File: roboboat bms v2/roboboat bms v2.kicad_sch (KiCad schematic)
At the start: 47 parts, among them J1 Conn_01x04_Pin, J2 XT90 Power Connector, J3 XT90 Power Connector, J4 BATT, J5 XT90 Power Connector, Q1 IRFP4468PbF, Q2 IRFP4468PbF, Q3 BSS84, Q4 IRFP4468PbF, Q5 IRFP4468PbF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

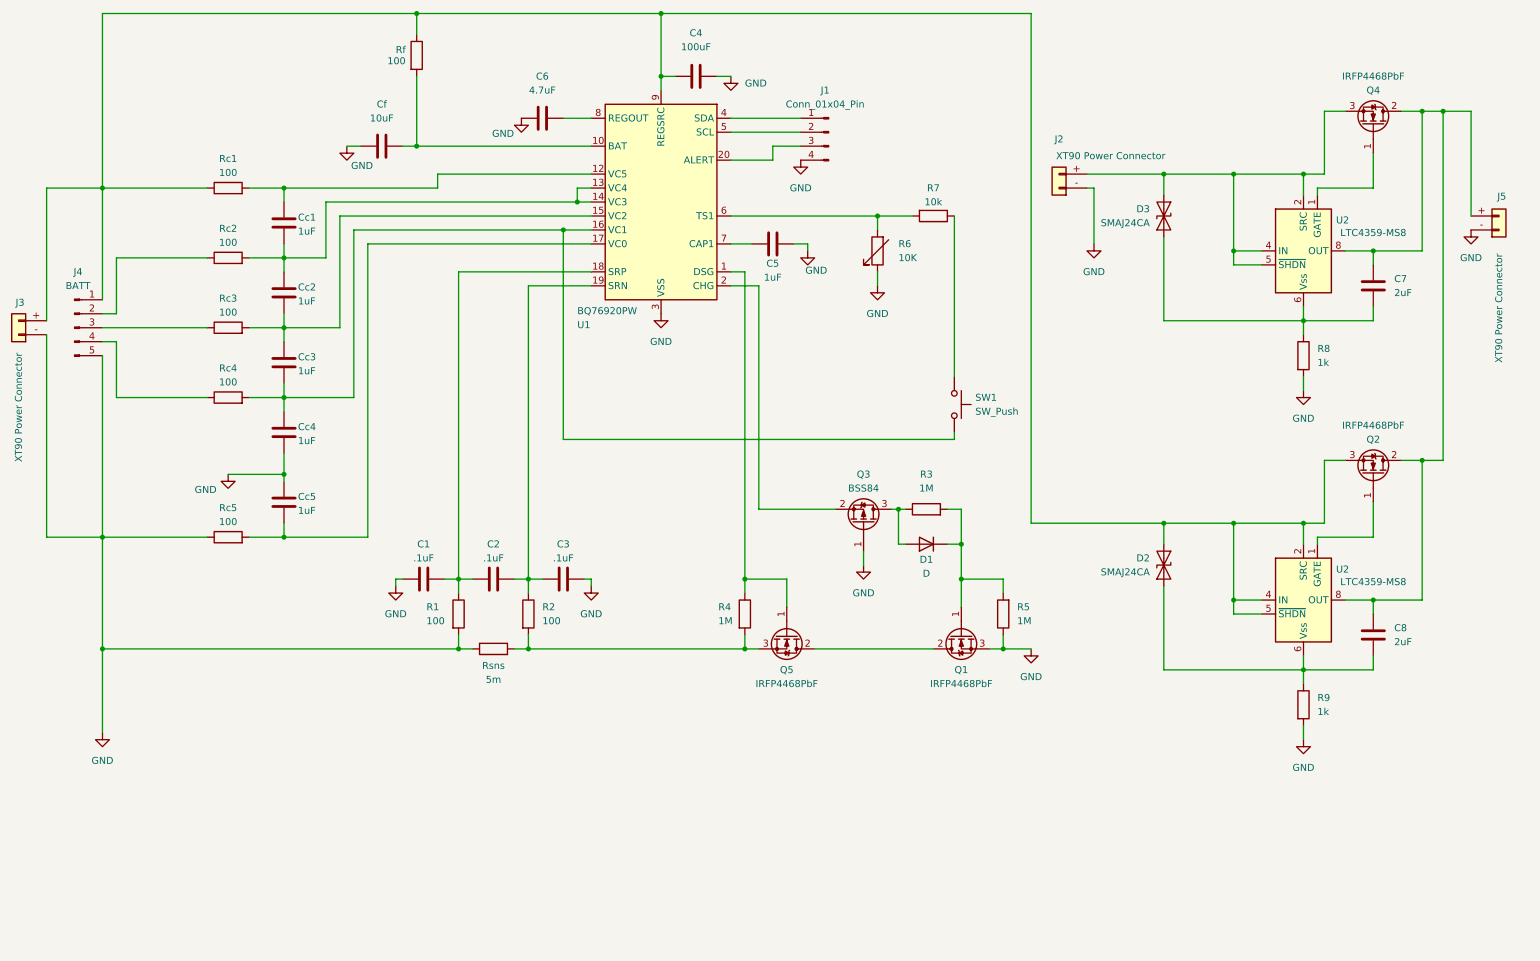
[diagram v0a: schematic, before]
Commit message: Update to new version of schematic Separate hotswap and BMS
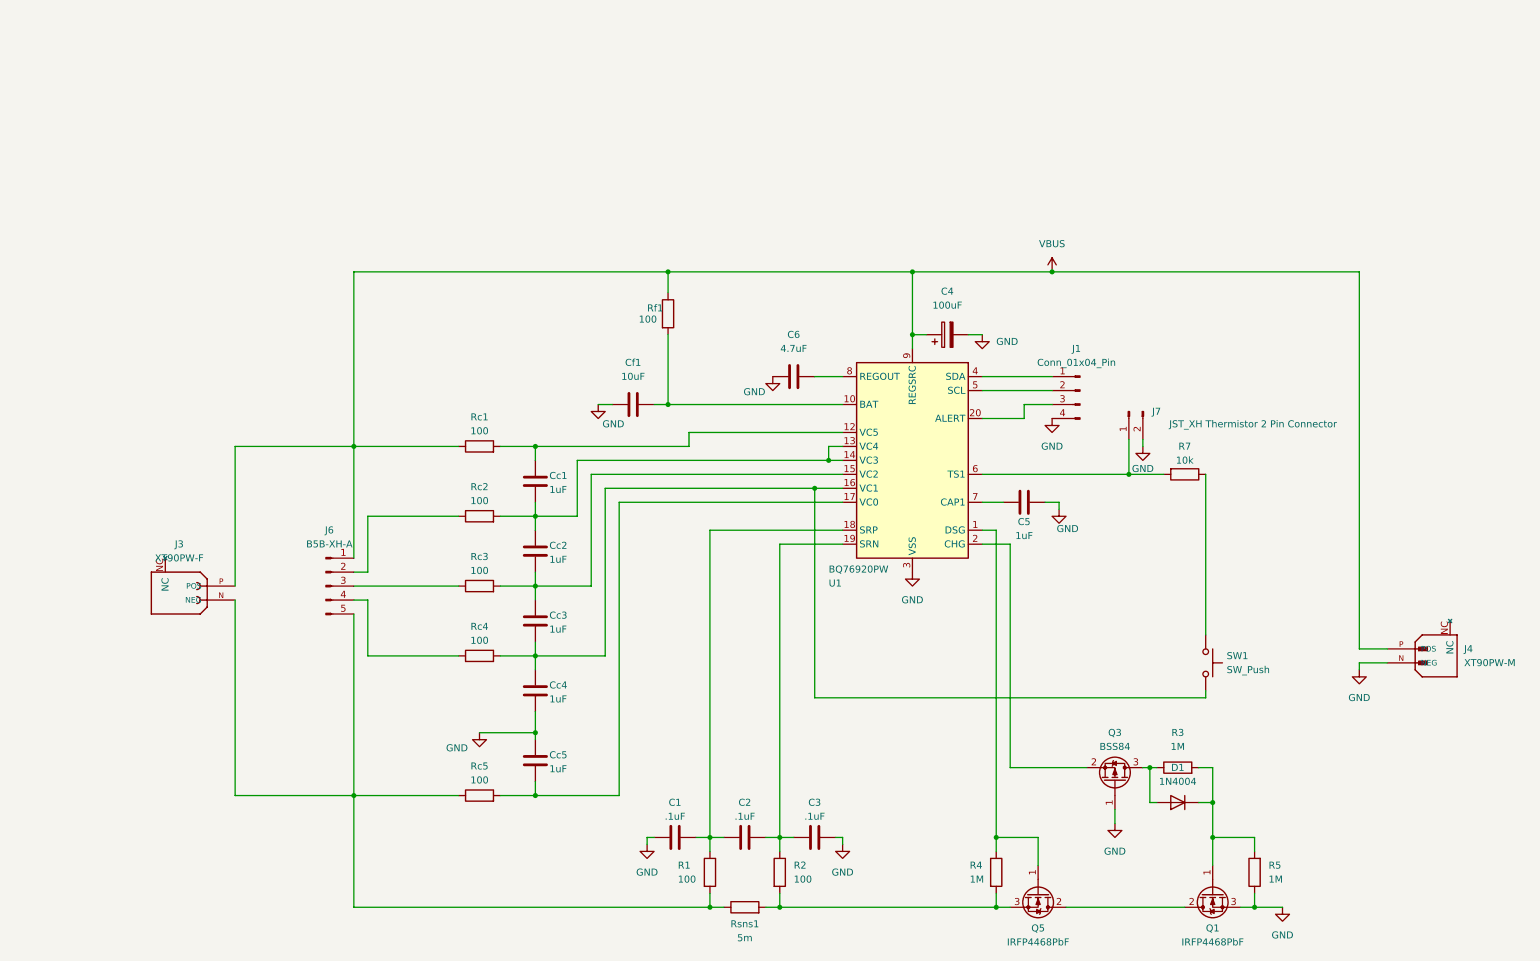
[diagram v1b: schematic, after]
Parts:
- removed C7, C8: 2uF, symbol Device:C
- removed D1: D, symbol Device:D
- removed D2, D3: SMAJ24CA, Diode_SMD:D_SMA, symbol Diode:SMAJ24CA
- removed J2, J3, J5: XT90 Power Connector, symbol Connector_Generic:Conn_01x02
- removed J4: BATT, symbol Connector:Conn_01x05_Pin
- removed Q2, Q4: IRFP4468PbF, Package_TO_SOT_THT:TO-247-3_Vertical, symbol Transistor_FET:IRFP4468PbF
- removed R6: 10K, symbol Device:R_Variable
- removed R8, R9: 1k, symbol Device:R
- removed U2 (x2): LTC4359-MS8, Package_SO:MSOP-8_3x3mm_P0.65mm, symbol Power_Management:LTC4359-MS8
- added D1: 1N4004, Diode_THT:D_DO-41_SOD81_P10.16mm_Horizontal, symbol Diode:1N4004
- added J3: XT90PW-F, footprints:AMASS_XT90PW-F, symbol XT90PW-F:XT90PW-F
- added J4: XT90PW-M, footprints:AMASS_XT90PW-M, symbol XT90PW-M:XT90PW-M
- added J6: B5B-XH-A, Connector_JST:JST_XH_B5B-XH-A_1x05_P2.50mm_Vertical, symbol Connector:Conn_01x05_Pin
- added J7: JST_XH Thermistor 2 Pin Connector, Connector_JST:JST_XH_B2B-XH-A_1x02_P2.50mm_Vertical, symbol Connector:Conn_01x02_Pin
- C1, C2, C3: footprint (none) -> Capacitor_SMD:C_0603_1608Metric; Link (none) -> https://mou.sr/3K4oacS; Mouser PN (none) -> 810-C1608X7R1H104K
- C4: footprint (none) -> Capacitor_THT:CP_Radial_D6.3mm_P2.50mm; symbol Device:C -> Device:C_Polarized; Link (none) -> https://mou.sr/49vdLRL; Mouser PN (none) -> 710-860010473007
- C5: footprint (none) -> Capacitor_SMD:C_0805_2012Metric; Link (none) -> https://mou.sr/4ayARnE; Mouser PN (none) -> 187-CL21B105KAFNNNG
- C6: footprint (none) -> Capacitor_SMD:C_1206_3216Metric; Link (none) -> https://mou.sr/4afC2vg; Mouser PN (none) -> 80-C1206C475K3PAC
- Cc1, Cc2, Cc3, Cc4, Cc5: footprint (none) -> Capacitor_SMD:C_0603_1608Metric; Link (none) -> https://mou.sr/4rhptG2; Mouser PN (none) -> 187-CL10A105KA8NFNC
- Cf1: renamed from Cf; footprint (none) -> Capacitor_SMD:C_1206_3216Metric; Link (none) -> https://mou.sr/4oaVgpa; Mouser PN (none) -> 963-TMK316BJ106KL-T
- J1: footprint (none) -> Connector_PinHeader_2.54mm:PinHeader_1x04_P2.54mm_Vertical; Notes (none) -> idk about this
- Q1, Q5: Link (none) -> https://mou.sr/3w4O2Ob; Mouser PN (none) -> 726-IRFP4468PBFXKMA1
- Q3: Link (none) -> https://mou.sr/48erSZg; Mouser PN (none) -> 512-BSS84
- R1, R2, Rc1, Rc2, Rc3, Rc4, Rc5: footprint (none) -> Resistor_SMD:R_1206_3216Metric; Link (none) -> https://mou.sr/4a8tGFK; Mouser PN (none) -> 603-RE1206FRE07100RL; Notes (none) -> no idea if this updated footprint name is right
- R3, R4, R5: footprint (none) -> Resistor_SMD:R_0603_1608Metric; Link (none) -> https://mou.sr/48r6KAp; Mouser PN (none) -> 71-CRCW0603-1.0M-E3
- R7: footprint (none) -> Resistor_SMD:R_0603_1608Metric; Link (none) -> https://mou.sr/44k2ZbH; Mouser PN (none) -> 755-ESR03EZPJ103
- Rf1: renamed from Rf; footprint (none) -> Resistor_SMD:R_1206_3216Metric; Link (none) -> https://mou.sr/4a8tGFK; Mouser PN (none) -> 603-RE1206FRE07100RL; Notes (none) -> no idea if this updated footprint name is right
- Rsns1: renamed from Rsns; footprint (none) -> Resistor_SMD:R_2512_6332Metric; Link (none) -> https://mou.sr/4rhQzNk; Mouser PN (none) -> 708-CSNL2512FTL500
- SW1: footprint (none) -> Button_Switch_THT:SW_PUSH_6mm; Link (none) -> https://mou.sr/4phQB5X; Mouser PN (none) -> 179-TS026660BK160LCR
- U1: Link (none) -> https://mou.sr/4r3TLMn; Mouser PN (none) -> 595-BQ7692003PW
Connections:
- net GND: now also J4.N (NEG), J7.2 (Pin_2); no longer R1.2, Rc5.1, Rsns1.1
- net at Rc2.1: now also J6.2 (Pin_2)
- net at R7.2, U1.6 (TS1): now also J7.1 (Pin_1)
- net VBUS: now reaches C4.1, Rc1.1, Rf1.1, U1.9 (REGSRC)
- net VBUS: now also J3.P (POS), J4.P (POS), J6.1 (Pin_1)
- net at Q3.3 (D), R3.1: now also D1.2 (A)
- net at Q1.1 (G), R3.2, R5.2: now also D1.1 (K)
- net at Rc3.1: now also J6.3 (Pin_3)
- net at Rc4.1: now also J6.4 (Pin_4)
- new net: J3.N (NEG), J6.5 (Pin_5), R1.2, Rc5.1, Rsns1.1
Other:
- moved on the sheet: C1, C2, C3, C5, C6, Cc1, Cc2, Cc3, Cc4, Cc5, Cf1, J1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

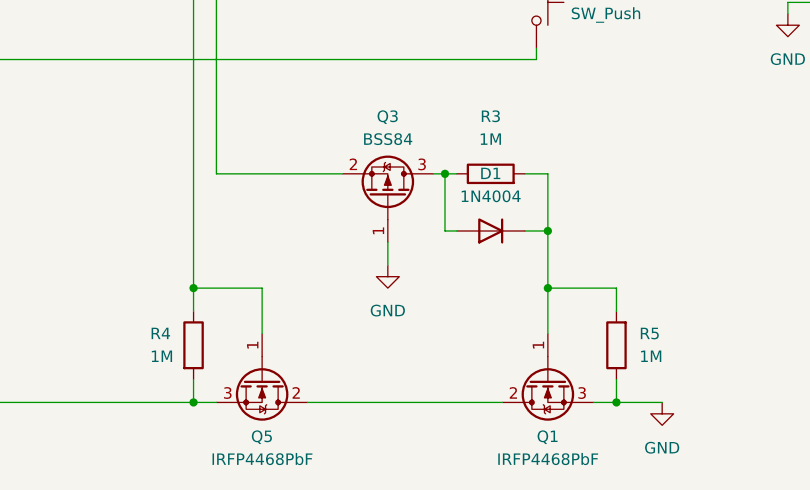
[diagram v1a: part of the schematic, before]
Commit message: update MOSFET to IRF7430
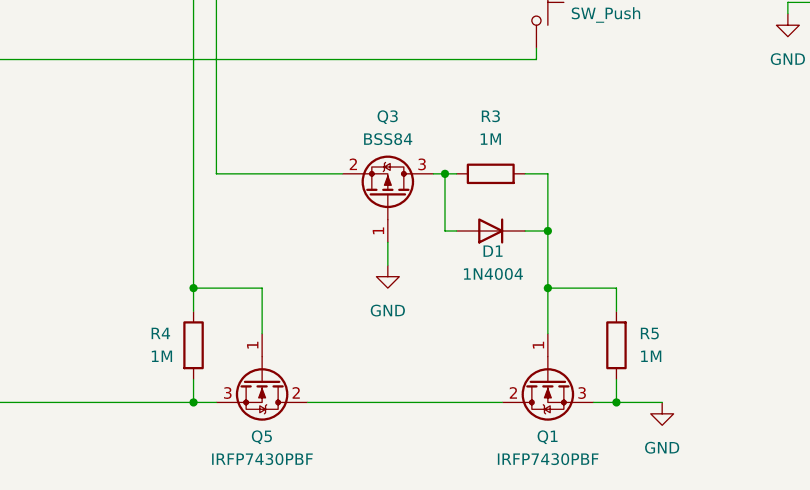
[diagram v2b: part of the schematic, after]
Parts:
- Q1, Q5: value IRFP4468PbF -> IRFP7430PBF; Link https://mou.sr/3w4O2Ob -> https://mou.sr/4j0VC0J; Mouser PN 726-IRFP4468PBFXKMA1 -> 942-IRFP7430PBF
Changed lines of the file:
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@@
 			)
 		)
-		(property "Value" "IRFP4468PbF"
+		(property "Value" "IRFP7430PBF"
 			(at 231.14 186.69 90)
 			(effects
@@
 			)
 		)
-		(property "Link" "https://mou.sr/3w4O2Ob"
+		(property "Link" "https://mou.sr/4j0VC0J"
 			(at 231.14 177.8 90)
 			(effects
@@
 			)
 		)
-		(property "Mouser PN" "726-IRFP4468PBFXKMA1 "
+		(property "Mouser PN" "942-IRFP7430PBF "
 			(at 231.14 177.8 90)
 			(effects
@@
 		(on_board yes)
 		(dnp no)
-		(fields_autoplaced yes)
 		(property "Reference" "D1"
-			(at 224.79 154.94 0)
+			(at 225.044 163.576 0)
 			(effects
 				(font
@@
 		)
 		(property "Value" "1N4004"
-			(at 224.79 157.48 0)
+			(at 225.044 166.116 0)
 			(effects
 				(font
@@
 			)
 		)
-		(property "Value" "IRFP4468PbF"
+		(property "Value" "IRFP7430PBF"
 			(at 199.39 186.69 90)
 			(effects
@@
 			)
 		)
-		(property "Link" "https://mou.sr/3w4O2Ob"
+		(property "Link" "https://mou.sr/4j0VC0J"
 			(at 199.39 177.8 90)
 			(effects
@@
 			)
 		)
-		(property "Mouser PN" "726-IRFP4468PBFXKMA1 "
+		(property "Mouser PN" "942-IRFP7430PBF "
 			(at 199.39 177.8 90)
 			(effects
